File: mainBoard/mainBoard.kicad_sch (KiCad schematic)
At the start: 28 parts, among them J1 Conn_01x01, J2 Conn_01x06_Male, J3 Conn_01x06_Male, J4 Conn_01x08_Female, Q1 SS8050-G, Q2 SS8050-G, SW1 SW_Push, SW2 SW_Push, U1 AMS1117-3.3, U2 ESP32-WROOM-E

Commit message: project restructured
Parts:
- added H1, H2, H3, H4: MountingHole, symbol Mechanical:MountingHole
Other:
- removed sheet IOBoard
- note added: "Mounting Holes"
- moved on the sheet: C6, C7, R5, R6, SW1, SW2

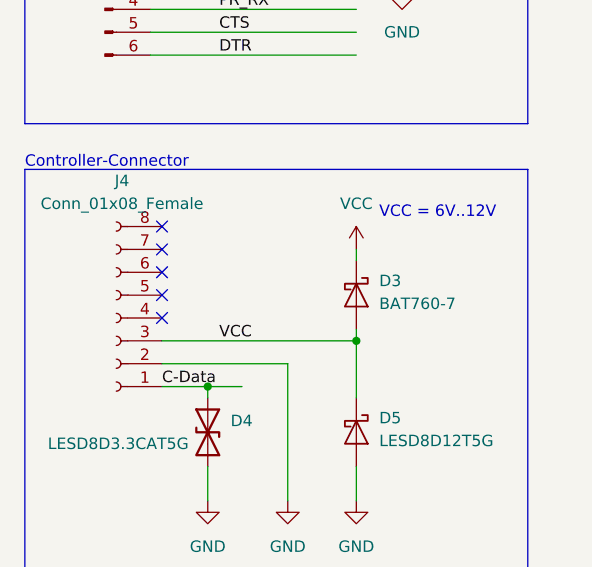
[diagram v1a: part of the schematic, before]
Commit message: added footprints to symbols
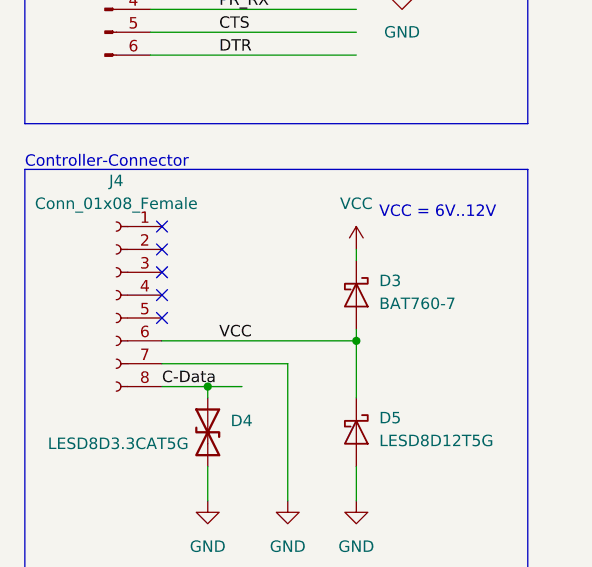
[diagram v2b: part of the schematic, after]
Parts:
- C1, C2, C4: footprint (none) -> Capacitor_SMD:C_0805_2012Metric
- C3, C5: footprint (none) -> Capacitor_SMD:C_0402_1005Metric
- C6, C7: footprint (none) -> Capacitor_SMD:C_0402_1005Metric_Pad0.74x0.62mm_HandSolder
- D1: footprint (none) -> LED_SMD:LED_0603_1608Metric
- D2, D3: footprint (none) -> Diode_SMD:D_SOD-323F
- D4, D5: footprint (none) -> SOD882:SOD882
- H1, H2, H3, H4: footprint (none) -> MountingHole:MountingHole_2.2mm_M2
- J1: footprint (none) -> Connector_Wire:SolderWire-0.25sqmm_1x01_D0.65mm_OD2mm
- J2, J3: footprint (none) -> Connector_JST:JST_XH_S6B-XH-A_1x06_P2.50mm_Horizontal
- J4: footprint (none) -> Connector_PinSocket_2.54mm:PinSocket_1x08_P2.54mm_Horizontal
- Q1, Q2: footprint (none) -> Package_TO_SOT_SMD:SOT-23-3
- R1, R2, R3, R4, R5, R6: footprint (none) -> Resistor_SMD:R_0402_1005Metric
- SW1, SW2: footprint (none) -> Button_Switch_SMD:SW_SPST_CK_RS282G05A3
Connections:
- net C-Data: now also J4.8 (Pin_8); no longer J4.1 (Pin_1)
- net GND: now also J4.7 (Pin_7); no longer J4.2 (Pin_2)
- net VCC: now also J4.6 (Pin_6); no longer J4.3 (Pin_3)
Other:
- moved on the sheet: J4

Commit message: new connector board
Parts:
- removed D3: BAT760-7, Diode_SMD:D_SOD-323F, symbol Diode:PMEG1020EH
- removed D4: LESD8D3.3CAT5G, SOD882:SOD882, symbol Diode:1N62xxCA
- removed D5: LESD8D12T5G, SOD882:SOD882, symbol Diode:PMEG1020EH
- removed J4: Conn_01x08_Female, Connector_PinSocket_2.54mm:PinSocket_1x08_P2.54mm_Horizontal, symbol Connector:Conn_01x08_Female
- added J4: Conn_01x03_Male, Connector_JST:JST_GH_SM03B-GHS-TB_1x03-1MP_P1.25mm_Horizontal, symbol Connector:Conn_01x03_Male
- J2, J3: footprint Connector_JST:JST_XH_S6B-XH-A_1x06_P2.50mm_Horizontal -> Connector_JST:JST_GH_SM06B-GHS-TB_1x06-1MP_P1.25mm_Horizontal
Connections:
- net C-Data: now also J4.2 (Pin_2)
- net GND: now also J4.3 (Pin_3)
- net VCC: now also J4.1 (Pin_1)
- no-connect marks 22 -> 17
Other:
- note added: "Connector-Port"
- note removed: "Controller-Connector"
- note removed: "VCC = 6V..12V"

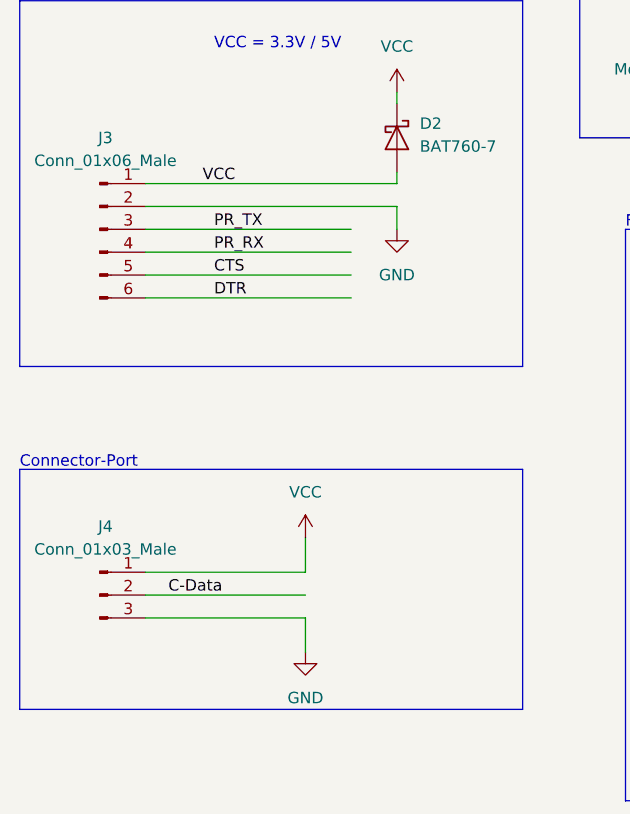
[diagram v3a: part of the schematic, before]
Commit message: main pcb rough alignment
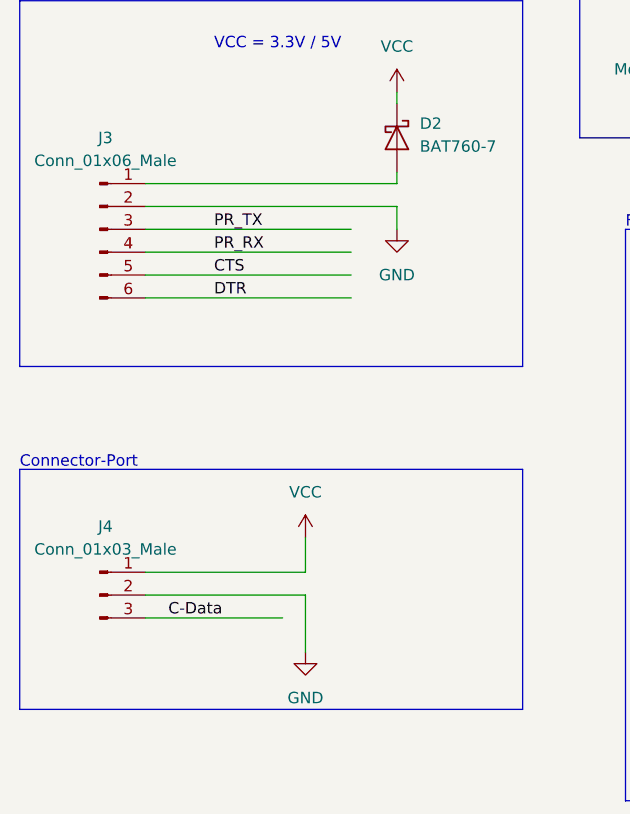
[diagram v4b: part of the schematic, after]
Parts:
- J2, J3: footprint Connector_JST:JST_GH_SM06B-GHS-TB_1x06-1MP_P1.25mm_Horizontal -> Connector_JST:JST_GH_BM06B-GHS-TBT_1x06-1MP_P1.25mm_Vertical
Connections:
- net C-Data: now also J4.3 (Pin_3); no longer J4.2 (Pin_2)
- net GND: now also J4.2 (Pin_2); no longer J4.3 (Pin_3)
- net VCC: no longer D2.2 (A), J3.1 (Pin_1)
- new net: D2.2 (A), J3.1 (Pin_1)
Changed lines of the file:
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@@
-    (stroke (width 0) (type default) (color 0 0 0 0))
-  )
-  (wire (pts (xy 31.75 173.99) (xy 49.53 173.99))
     (stroke (width 0) (type default) (color 0 0 0 0))
   )
@@
     (stroke (width 0) (type default) (color 0 0 0 0))
   )
+  (wire (pts (xy 31.75 173.99) (xy 46.99 173.99))
+    (stroke (width 0) (type default) (color 0 0 0 0))
+  )
   (wire (pts (xy 62.23 87.63) (xy 62.23 88.9))
     (stroke (width 0) (type default) (color 0 0 0 0))
@@
     (stroke (width 0) (type default) (color 0 0 0 0))
   )
-  (wire (pts (xy 49.53 173.99) (xy 49.53 177.8))
-    (stroke (width 0) (type default) (color 0 0 0 0))
-  )
   (wire (pts (xy 232.41 151.13) (xy 232.41 154.94))
     (stroke (width 0) (type default) (color 0 0 0 0))
@@
   )
   (wire (pts (xy 31.75 133.35) (xy 54.61 133.35))
+    (stroke (width 0) (type default) (color 0 0 0 0))
+  )
+  (wire (pts (xy 49.53 171.45) (xy 49.53 177.8))
     (stroke (width 0) (type default) (color 0 0 0 0))
   )
@@
     (effects (font (size 1.27 1.27)) (justify left bottom))
   )
-  (label "C-Data" (at 34.29 171.45 0)
-    (effects (font (size 1.27 1.27)) (justify left bottom))
-  )
-  (label "VCC" (at 38.1 125.73 0)
+  (label "C-Data" (at 34.29 173.99 0)
     (effects (font (size 1.27 1.27)) (justify left bottom))
   )
@@
     (property "Reference" "J3" (id 0) (at 27.305 120.65 0))
     (property "Value" "Conn_01x06_Male" (id 1) (at 27.305 123.19 0))
-    (property "Footprint" "Connector_JST:JST_GH_SM06B-GHS-TB_1x06-1MP_P1.25mm_Horizontal" (id 2) (at 26.67 130.81 0)
+    (property "Footprint" "Connector_JST:JST_GH_BM06B-GHS-TBT_1x06-1MP_P1.25mm_Vertical" (id 2) (at 26.67 130.81 0)
       (effects (font (size 1.27 1.27)) hide)
     )
@@
     (property "Reference" "J2" (id 0) (at 28.575 80.01 0))
     (property "Value" "Conn_01x06_Male" (id 1) (at 28.575 82.55 0))
-    (property "Footprint" "Connector_JST:JST_GH_SM06B-GHS-TB_1x06-1MP_P1.25mm_Horizontal" (id 2) (at 27.94 90.17 0)
+    (property "Footprint" "Connector_JST:JST_GH_BM06B-GHS-TBT_1x06-1MP_P1.25mm_Vertical" (id 2) (at 27.94 90.17 0)
       (effects (font (size 1.27 1.27)) hide)
     )
@@
     )
     (path "/d8fdcbf8-9d96-4eb1-a1b7-f7cd518ce4ae"
-      (reference "J2") (unit 1) (value "Conn_01x06_Male") (footprint "Connector_JST:JST_GH_SM06B-GHS-TB_1x06-1MP_P1.25mm_Horizontal")
+      (reference "J2") (unit 1) (value "Conn_01x06_Male") (footprint "Connector_JST:JST_GH_BM06B-GHS-TBT_1x06-1MP_P1.25mm_Vertical")
     )
     (path "/049689ed-e259-4325-9043-9efcc09750c1"
-      (reference "J3") (unit 1) (value "Conn_01x06_Male") (footprint "Connector_JST:JST_GH_SM06B-GHS-TB_1x06-1MP_P1.25mm_Horizontal")
+      (reference "J3") (unit 1) (value "Conn_01x06_Male") (footprint "Connector_JST:JST_GH_BM06B-GHS-TBT_1x06-1MP_P1.25mm_Vertical")
     )
     (path "/085255d2-4136-46b4-b559-656cd8f2bb36"

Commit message: io board pcb created
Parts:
- SW1, SW2: value SW_Push -> C520860
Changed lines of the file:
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@@
     (in_bom yes) (on_board yes) (fields_autoplaced)
     (property "Reference" "SW2" (id 0) (at 238.76 135.89 0))
-    (property "Value" "SW_Push" (id 1) (at 238.76 138.43 0))
+    (property "Value" "C520860" (id 1) (at 238.76 138.43 0))
     (property "Footprint" "Button_Switch_SMD:SW_SPST_CK_RS282G05A3" (id 2) (at 238.76 138.43 0)
       (effects (font (size 1.27 1.27)) hide)
@@
     (in_bom yes) (on_board yes) (fields_autoplaced)
     (property "Reference" "SW1" (id 0) (at 194.31 135.89 0))
-    (property "Value" "SW_Push" (id 1) (at 194.31 138.43 0))
+    (property "Value" "C520860" (id 1) (at 194.31 138.43 0))
     (property "Footprint" "Button_Switch_SMD:SW_SPST_CK_RS282G05A3" (id 2) (at 194.31 138.43 0)
       (effects (font (size 1.27 1.27)) hide)
@@
     )
     (path "/eca37a6a-4133-4eaf-8ed7-46ece9855ada"
-      (reference "SW1") (unit 1) (value "SW_Push") (footprint "Button_Switch_SMD:SW_SPST_CK_RS282G05A3")
+      (reference "SW1") (unit 1) (value "C520860") (footprint "Button_Switch_SMD:SW_SPST_CK_RS282G05A3")
     )
     (path "/add678d2-2796-47c4-bb79-f2bbcac2aff2"
-      (reference "SW2") (unit 1) (value "SW_Push") (footprint "Button_Switch_SMD:SW_SPST_CK_RS282G05A3")
+      (reference "SW2") (unit 1) (value "C520860") (footprint "Button_Switch_SMD:SW_SPST_CK_RS282G05A3")
     )
     (path "/9a64a489-0d38-49e0-99a9-8ea8688ac770"

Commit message: connector and emitter switched
maybe a problem maybe not
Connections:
- net Boot: now also Q2.3 (C); no longer Q2.2 (E)
- net DTR: now also Q2.2 (E); no longer Q2.3 (C)
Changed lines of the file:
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@@
     (pin "1")
   )
-  (symbol (lib_id "Device:Q_NPN_BEC") (at 129.54 176.53 0) (unit 1)
+  (symbol (lib_id "Device:Q_NPN_BEC") (at 129.54 176.53 0) (mirror x) (unit 1)
     (in_bom yes) (on_board yes) (fields_autoplaced)
-    (property "Reference" "Q2" (id 0) (at 134.62 175.2599 0)
+    (property "Reference" "Q2" (id 0) (at 134.62 177.8001 0)
       (effects (font (size 1.27 1.27)) (justify left))
     )
-    (property "Value" "SS8050-G" (id 1) (at 134.62 177.7999 0)
+    (property "Value" "SS8050-G" (id 1) (at 134.62 175.2601 0)
       (effects (font (size 1.27 1.27)) (justify left))
     )
-    (property "Footprint" "Package_TO_SOT_SMD:SOT-23-3" (id 2) (at 134.62 173.99 0)
+    (property "Footprint" "Package_TO_SOT_SMD:SOT-23-3" (id 2) (at 134.62 179.07 0)
       (effects (font (size 1.27 1.27)) hide)
     )
